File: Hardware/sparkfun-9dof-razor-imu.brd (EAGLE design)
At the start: 31.8 x 31.8 mm, 57 parts, among them J1 LiPo, J3 USD_CONNECTOR, U1 3.3V, U2 MCP73831, U3 MPU-9250, U4 ATSAMD21G-A, Y1 32.768kHz

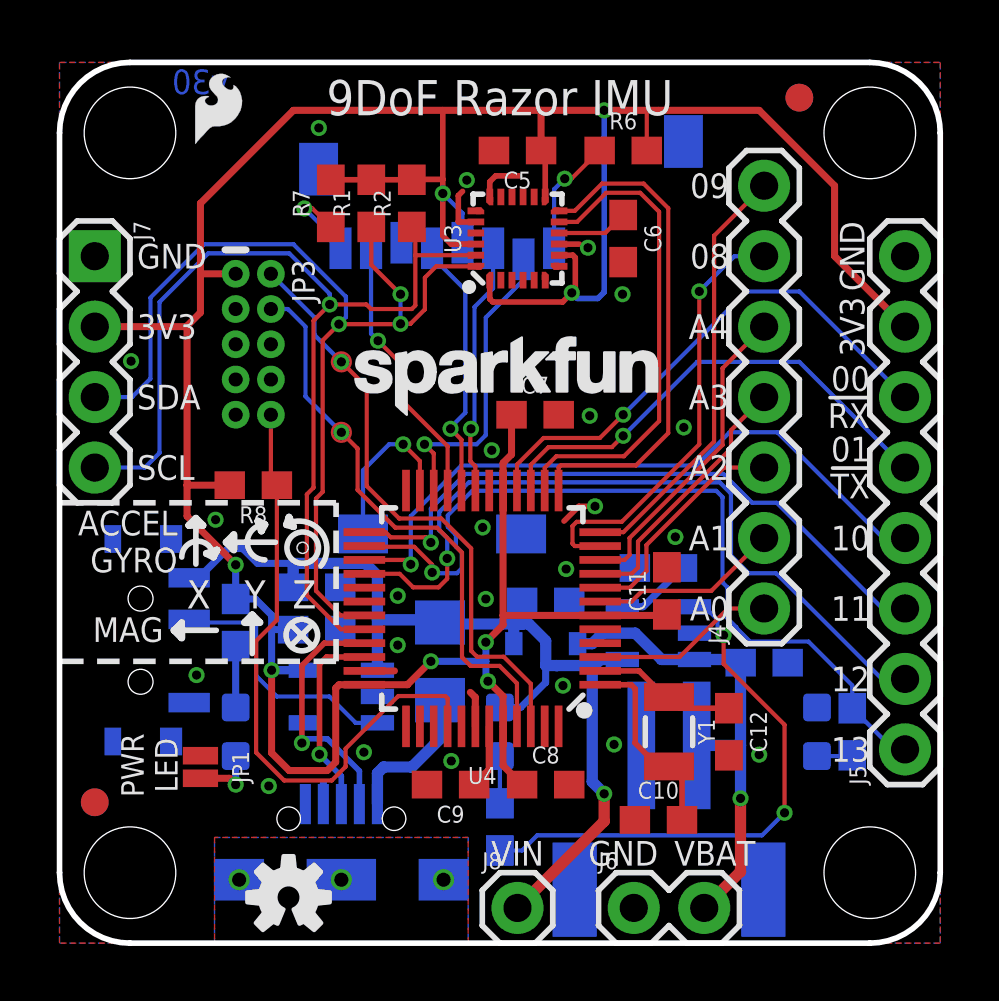
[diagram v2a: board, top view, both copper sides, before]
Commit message: Checklist adjustments - mostly silkscreen nudging.
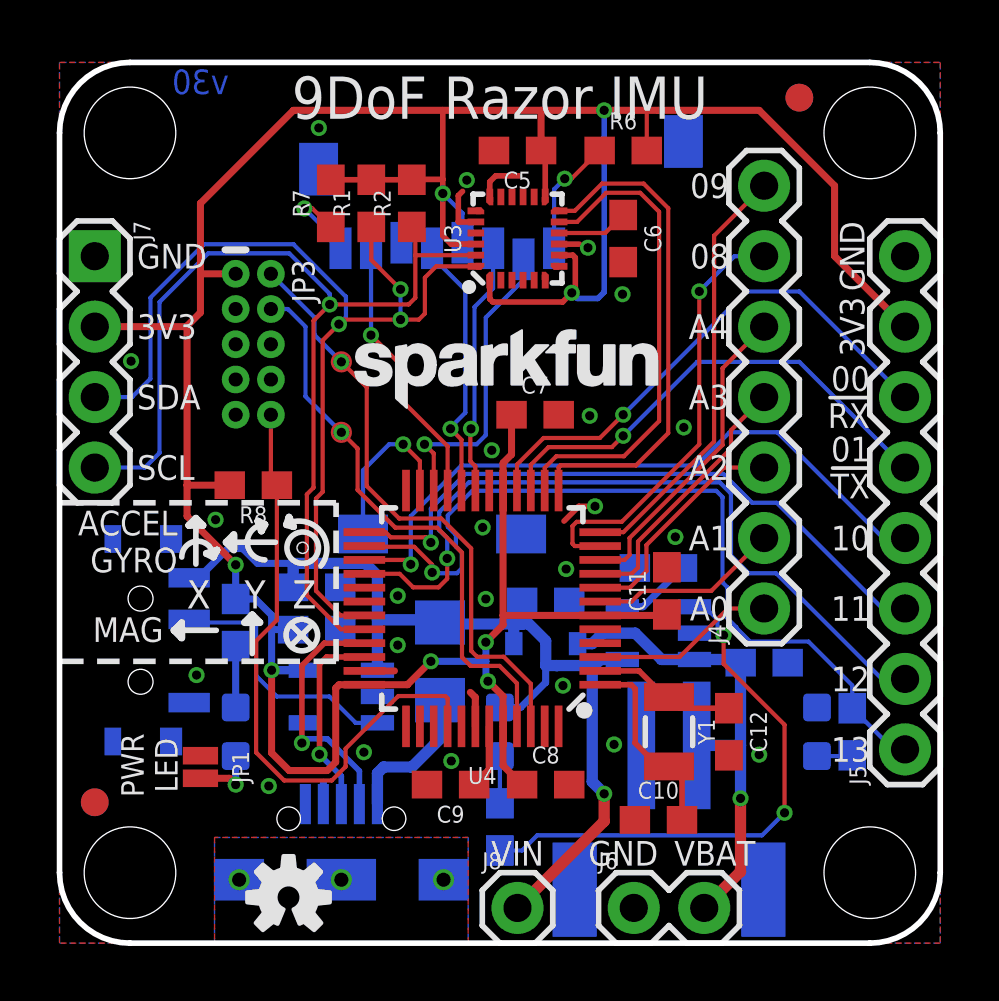
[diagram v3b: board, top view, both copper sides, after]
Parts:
- removed LOGO4: SFE_LOGO_FLAME.1_INCH, SparkFun-Aesthetics:SFE_LOGO_FLAME_.1
- moved LOGO3 0.25 mm to (10.2, 18.8)
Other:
- board text added: "http://sfe.io/t567"
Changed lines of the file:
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@@
 <setting verticaltext="up"/>
 </settings>
-<grid distance="0.05" unitdist="inch" unit="inch" style="lines" multiple="1" display="yes" altdistance="0.001" altunitdist="inch" altunit="inch"/>
+<grid distance="0.05" unitdist="inch" unit="inch" style="lines" multiple="1" display="yes" altdistance="0.005" altunitdist="inch" altunit="inch"/>
 <layers>
 <layer number="1" name="Top" color="4" fill="1" visible="yes" active="yes"/>
@@
 <text x="2.794" y="19.685" size="0.889" layer="21" font="vector" ratio="15" align="center-left">SDA</text>
 <text x="2.794" y="17.145" size="0.889" layer="21" font="vector" ratio="15" align="center-left">SCL</text>
-<text x="15.875" y="29.845" size="1.27" layer="21" font="vector" ratio="15" rot="R180" align="top-center">9DoF Razor IMU</text>
-<text x="5.08" y="24.765" size="0.889" layer="22" font="vector" ratio="15" rot="MR0" align="center-left">GND</text>
-<text x="5.461" y="22.225" size="0.889" layer="22" font="vector" ratio="15" rot="MR0" align="center-left">3.3V</text>
-<text x="5.08" y="19.685" size="0.889" layer="22" font="vector" ratio="15" rot="MR0" align="center-left">SDA</text>
-<text x="5.08" y="17.145" size="0.889" layer="22" font="vector" ratio="15" rot="MR0" align="center-left">SCL</text>
+<text x="15.875" y="29.718" size="1.524" layer="21" font="vector" ratio="15" rot="R180" align="top-center">9DoF Razor IMU</text>
+<text x="2.3622" y="24.8412" size="0.889" layer="22" font="vector" ratio="15" rot="MR180" align="center-left">GND</text>
+<text x="2.3622" y="22.3012" size="0.889" layer="22" font="vector" ratio="15" rot="MR180" align="center-left">3.3V</text>
+<text x="2.3622" y="19.7612" size="0.889" layer="22" font="vector" ratio="15" rot="MR180" align="center-left">SDA</text>
+<text x="2.3622" y="17.2212" size="0.889" layer="22" font="vector" ratio="15" rot="MR180" align="center-left">SCL</text>
 <text x="5.08" y="31.496" size="0.889" layer="16" font="vector" ratio="15" rot="MR180" align="bottom-center">v30</text>
 <text x="0.254" y="13.97" size="0.889" layer="22" font="vector" ratio="15" rot="MR90" align="bottom-center">ON</text>
@@
 <wire x1="0.381" y1="12.319" x2="1.143" y2="12.319" width="0.508" layer="22"/>
 <wire x1="1.143" y1="12.319" x2="0.762" y2="12.7" width="0.508" layer="22"/>
-<text x="27.178" y="6.0325" size="0.889" layer="22" font="vector" ratio="15" rot="MR0" align="top-center">13</text>
+<text x="30.48" y="5.8039" size="0.889" layer="22" font="vector" ratio="15" rot="MR0" align="top-center">13</text>
 <text x="15.875" y="9.144" size="0.889" layer="22" font="vector" ratio="15" rot="MR180" align="top-center">CHG</text>
 <text x="6.35" y="9.144" size="0.889" layer="22" font="vector" ratio="15" rot="MR180" align="top-center">PWR</text>
@@
 <text x="26.67" y="14.6685" size="0.889" layer="22" font="vector" ratio="15" rot="MR90" align="bottom-center">A1</text>
 <text x="26.67" y="12.1285" size="0.889" layer="22" font="vector" ratio="15" rot="MR90" align="bottom-center">A0</text>
+<text x="15.875" y="31.369" size="1.016" layer="22" font="vector" ratio="15" rot="MR0" align="top-center">http://sfe.io/t567</text>
 </plain>
 <attributes>
@@
 <element name="LOGO1" library="SparkFun-Aesthetics" package="SFE_LOGO_FLAME_.1" value="SFE_LOGO_FLAME.1_INCH" x="7.747" y="26.797" rot="MR0"/>
 <element name="LOGO2" library="SparkFun-Aesthetics" package="OSHW-LOGO-S" value="OSHW-LOGOS" x="8.255" y="1.651"/>
-<element name="LOGO3" library="SparkFun-Aesthetics" package="SFE_LOGO_NAME_.1" value="SFE_LOGO_NAME.1_INCH" x="10.16" y="18.542"/>
+<element name="LOGO3" library="SparkFun-Aesthetics" package="SFE_LOGO_NAME_.1" value="SFE_LOGO_NAME.1_INCH" x="10.16" y="18.796"/>
 <element name="J3" library="SparkFun-Connectors" package="MICRO-SD-SOCKET-PP" value="USD_CONNECTOR" x="8.89" y="14.351" rot="MR0">
 <attribute name="PROD_ID" value="CONN-07820" x="8.89" y="14.351" size="1.778" layer="28" font="vector" ratio="15" rot="MR0" display="off"/>
@@
 <element name="TP1" library="SparkFun-Connectors" package="PAD.03X.03" value="TEST-POINT3" x="10.16" y="18.415"/>
 <element name="TP2" library="SparkFun-Connectors" package="PAD.03X.03" value="TEST-POINT3" x="10.16" y="20.955"/>
-<element name="LOGO4" library="SparkFun-Aesthetics" package="SFE_LOGO_FLAME_.1" value="SFE_LOGO_FLAME.1_INCH" x="4.572" y="28.448"/>
 </elements>
 <signals>
@@
 <wire x1="9.2456" y1="16.0274" x2="9.4869" y2="16.2687" width="0.1524" layer="1"/>
 <wire x1="9.4869" y1="16.2687" x2="9.4869" y2="21.7297" width="0.1524" layer="1"/>
-<via x="12.2936" y="23.3934" extent="1-16" drill="0.3302"/>
-<via x="12.2936" y="22.3266" extent="1-16" drill="0.3302"/>
-<wire x1="11.2395" y1="25.82" x2="11.2395" y2="24.4475" width="0.1524" layer="1"/>
-<wire x1="12.2936" y1="23.3934" x2="12.2936" y2="22.3266" width="0.1524" layer="16"/>
+<via x="12.2936" y="23.5712" extent="1-16" drill="0.3302"/>
+<via x="12.2936" y="22.479" extent="1-16" drill="0.3302"/>
+<wire x1="11.2395" y1="25.82" x2="11.2395" y2="24.6253" width="0.1524" layer="1"/>
 <via x="10.0711" y="22.3139" extent="1-16" drill="0.3302"/>
-<wire x1="12.2936" y1="22.3266" x2="12.6492" y2="22.3266" width="0.1524" layer="1"/>
-<wire x1="12.6492" y1="22.3266" x2="13.1699" y2="22.8473" width="0.1524" layer="1"/>
-<wire x1="13.1699" y1="22.8473" x2="13.1699" y2="23.9903" width="0.1524" layer="1"/>
 <wire x1="13.1699" y1="23.9903" x2="13.5796" y2="24.4" width="0.1524" layer="1"/>
 <wire x1="14.9575" y1="24.4" x2="13.5796" y2="24.4" width="0.1524" layer="1"/>
-<wire x1="12.2936" y1="23.3934" x2="11.2395" y2="24.4475" width="0.1524" layer="1"/>
+<wire x1="12.2936" y1="23.5712" x2="11.2395" y2="24.6253" width="0.1524" layer="1"/>
 <wire x1="8.4328" y1="25.1968" x2="5.207" y2="25.1968" width="0.1524" layer="16"/>
 <wire x1="5.207" y1="25.1968" x2="3.2766" y2="23.2664" width="0.1524" layer="16"/>
@@
 <wire x1="10.3251" y1="23.3045" x2="10.3251" y2="22.5679" width="0.1524" layer="16"/>
 <wire x1="10.3251" y1="22.5679" x2="10.0711" y2="22.3139" width="0.1524" layer="16"/>
-<wire x1="10.0711" y1="22.3139" x2="12.2809" y2="22.3139" width="0.1524" layer="1"/>
-<wire x1="12.2809" y1="22.3139" x2="12.2936" y2="22.3266" width="0.1524" layer="1"/>
+<wire x1="12.2936" y1="22.479" x2="12.2936" y2="23.5712" width="0.1524" layer="16"/>
+<wire x1="13.1699" y1="23.9903" x2="13.1699" y2="22.6949" width="0.1524" layer="1"/>
+<wire x1="13.1699" y1="22.6949" x2="12.954" y2="22.479" width="0.1524" layer="1"/>
+<wire x1="12.954" y1="22.479" x2="12.2936" y2="22.479" width="0.1524" layer="1"/>
+<wire x1="12.2936" y1="22.479" x2="10.2362" y2="22.479" width="0.1524" layer="1"/>
+<wire x1="10.2362" y1="22.479" x2="10.0711" y2="22.3139" width="0.1524" layer="1"/>
 </signal>
 <signal name="SCL">
@@
 <wire x1="9.1567" y1="16.4211" x2="9.1567" y2="22.4409" width="0.1524" layer="1"/>
 <wire x1="12.7" y1="25.7144" x2="12.7" y2="25.82" width="0.1524" layer="1"/>
-<wire x1="12.7" y1="22.86" x2="11.2268" y2="22.86" width="0.1524" layer="1"/>
 <wire x1="9.1567" y1="22.4409" x2="9.7409" y2="23.0251" width="0.1524" layer="1"/>
 <via x="9.7409" y="23.0251" extent="1-16" drill="0.3302"/>
-<wire x1="12.7" y1="22.86" x2="12.827" y2="22.987" width="0.1524" layer="1"/>
-<wire x1="12.827" y1="22.987" x2="12.827" y2="24.8" width="0.1524" layer="1"/>
 <wire x1="12.827" y1="24.8" x2="15.01" y2="24.8" width="0.1524" layer="1"/>
 <wire x1="12.7" y1="25.7144" x2="12.827" y2="25.5874" width="0.1524" layer="1"/>
@@
 <wire x1="1.27" y1="17.145" x2="3.0734" y2="17.145" width="0.1524" layer="16"/>
 <wire x1="3.0734" y1="17.145" x2="3.6068" y2="17.6784" width="0.1524" layer="16"/>
-<wire x1="9.7409" y1="23.0251" x2="11.0617" y2="23.0251" width="0.1524" layer="1"/>
-<wire x1="11.0617" y1="23.0251" x2="11.2268" y2="22.86" width="0.1524" layer="1"/>
+<wire x1="9.7409" y1="23.0251" x2="12.5857" y2="23.0251" width="0.1524" layer="1"/>
+<wire x1="12.5857" y1="23.0251" x2="12.827" y2="23.2664" width="0.1524" layer="1"/>
+<wire x1="12.827" y1="23.2664" x2="12.827" y2="24.8" width="0.1524" layer="1"/>
 </signal>
 <signal name="N$1">
@@
 <contactref element="J3" pad="DO"/>
 <wire x1="13.99" y1="16.315" x2="13.99" y2="17.9124" width="0.1524" layer="1"/>
-<wire x1="11.4808" y1="21.717" x2="11.23" y2="21.9678" width="0.1524" layer="16"/>
-<wire x1="11.23" y1="21.9678" x2="11.23" y2="25.051" width="0.1524" layer="16"/>
-<via x="11.4808" y="21.717" extent="1-16" drill="0.3302"/>
+<wire x1="11.2268" y1="21.9202" x2="11.23" y2="21.917" width="0.1524" layer="16"/>
+<wire x1="11.23" y1="21.917" x2="11.23" y2="25.051" width="0.1524" layer="16"/>
+<via x="11.2268" y="21.9202" extent="1-16" drill="0.3302"/>
 <wire x1="13.99" y1="17.9124" x2="12.3698" y2="19.5326" width="0.1524" layer="1"/>
-<wire x1="12.3698" y1="19.5326" x2="12.3698" y2="20.828" width="0.1524" layer="1"/>
-<wire x1="12.3698" y1="20.828" x2="11.4808" y2="21.717" width="0.1524" layer="1"/>
+<wire x1="12.3698" y1="19.5326" x2="12.3698" y2="20.7772" width="0.1524" layer="1"/>
+<wire x1="12.3698" y1="20.7772" x2="11.2268" y2="21.9202" width="0.1524" layer="1"/>
 </signal>
 <signal name="SD_!CS!">

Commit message: Value Added to .brd File
Right Angle Slide Switch Added for 3D Modeling
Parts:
- S1: value (none) -> SWITCH-SPST-SMD-A
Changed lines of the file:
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@@
 <?xml version="1.0" encoding="utf-8"?>
 <!DOCTYPE eagle SYSTEM "eagle.dtd">
-<eagle version="7.5.0">
+<eagle version="7.7.0">
 <drawing>
 <settings>
@@
 <element name="H4" library="SparkFun-Electromechanical" package="STAND-OFF" value="STAND-OFF" x="2.54" y="29.21"/>
 <element name="H3" library="SparkFun-Electromechanical" package="STAND-OFF" value="STAND-OFF" x="29.21" y="29.21"/>
-<element name="S1" library="SparkFun-Electromechanical" package="SWITCH-SPST-SMD-A" value="" x="2.921" y="10.922" rot="MR270">
+<element name="S1" library="SparkFun-Electromechanical" package="SWITCH-SPST-SMD-A" value="SWITCH-SPST-SMD-A" x="2.921" y="10.922" rot="MR270">
 <attribute name="PROD_ID" value="SWCH-10651" x="2.921" y="10.922" size="1.778" layer="28" font="vector" ratio="15" rot="MR270" display="off"/>
 </element>
